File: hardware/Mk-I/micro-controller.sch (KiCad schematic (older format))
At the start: 29 parts, among them U10 STM32_SWD_Connector, U4 STM32F407VG, U8 MOLEX_microSD_47219-2001, X1 CRYSTAL

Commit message: Cleanup schematics
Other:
- note added: "Debug port"
- note added: "I2C pull-ups"
- note added: "SD card"
- moved on the sheet: U10, U8

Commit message: HW: Add a DFU mode switch
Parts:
- added DFU_MODE1: Jumper_NO_Small, Buttons_Switches_SMD:SW_SPST_EVQP7A, symbol Jumper_NO_Small
- C12, C13, C14, C15, C16, C17, C18, C19, C20, C21, C22, C23, C24, C4, C5: symbol C -> C-RESCUE-wnm_mk_1
- R10, R11, R12, R13, R14, R3, R4, R5, R6: symbol R -> R-RESCUE-wnm_mk_1
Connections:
- net labels added: BOOT0
- wire segments 44 -> 45

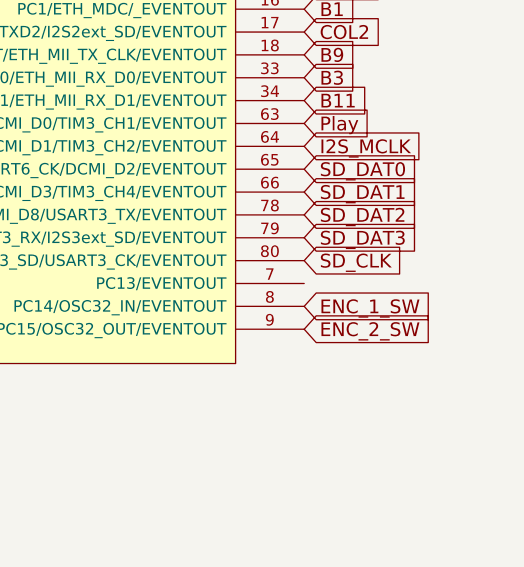
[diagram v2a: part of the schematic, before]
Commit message: HW: Add screen reset line and some ground path tweaking
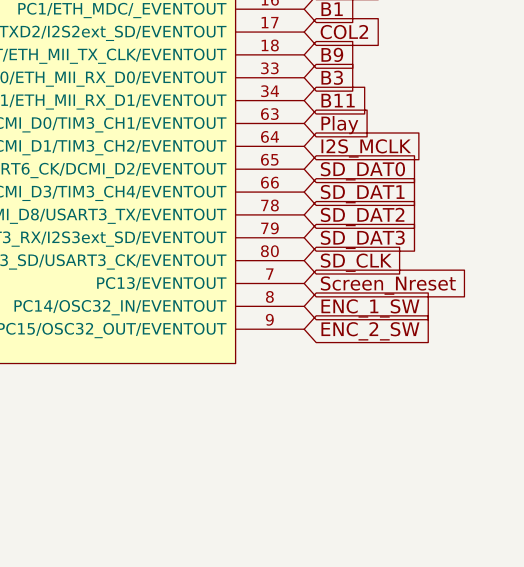
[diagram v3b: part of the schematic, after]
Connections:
- net Screen_Nreset: now reaches U4.7 (PC13/EVENTOUT)
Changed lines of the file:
@@
 Text GLabel 2300 1800 2    60   Input ~ 0
 3V3
+Text GLabel 12850 7200 2    60   Input ~ 0
+Screen_Nreset
 $EndSCHEMATC

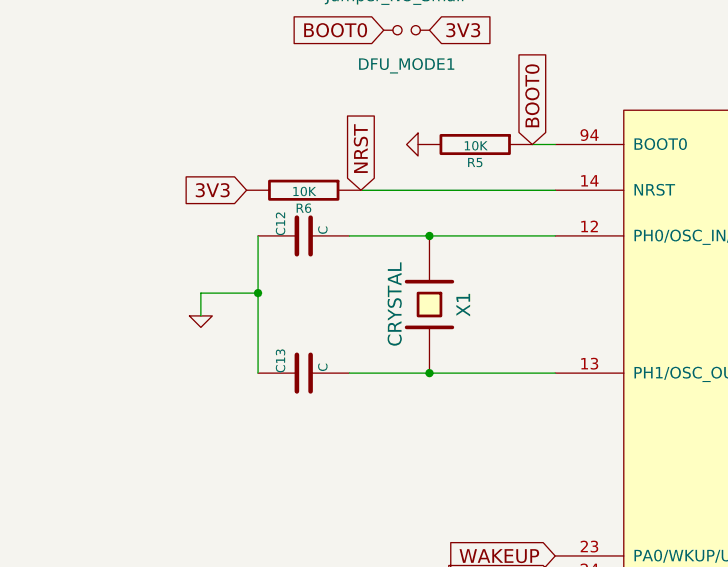
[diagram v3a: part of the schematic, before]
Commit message: HW: Start Mk-I rev-A known problems
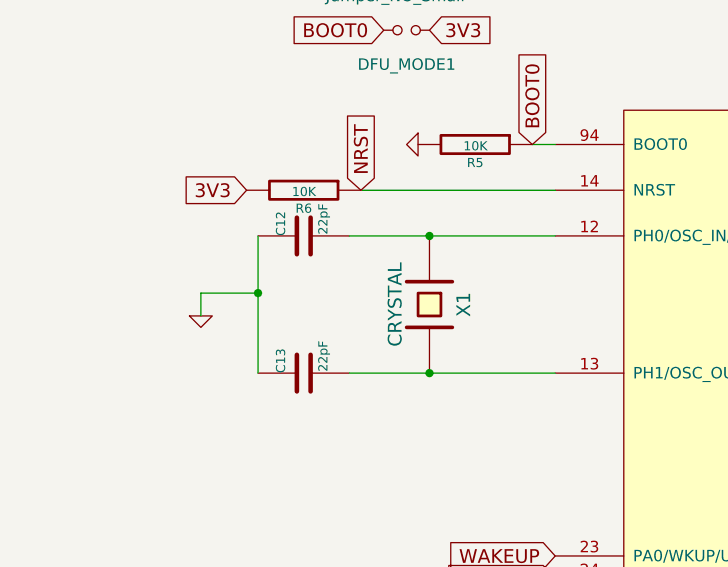
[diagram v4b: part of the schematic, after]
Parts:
- C12, C13: value C -> 22pF
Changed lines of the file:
@@
 AR Path="/585DBE08/585F8833" Ref="C12"  Part="1"
 F 0 "C12" H 1750 2800 40  0000 L CNN
-F 1 "C" H 1756 2615 40  0000 L CNN
+F 1 "22pF" H 1756 2615 40  0000 L CNN
 F 2 "Capacitors_SMD:C_0805" H 1788 2550 30  0001 C CNN
 F 3 "" H 1750 2700 60  0000 C CNN
@@
 AR Path="/585DBE08/585F888D" Ref="C13"  Part="1"
 F 0 "C13" H 1750 3400 40  0000 L CNN
-F 1 "C" H 1756 3215 40  0000 L CNN
+F 1 "22pF" H 1756 3215 40  0000 L CNN
 F 2 "Capacitors_SMD:C_0805" H 1788 3150 30  0001 C CNN
 F 3 "" H 1750 3300 60  0000 C CNN

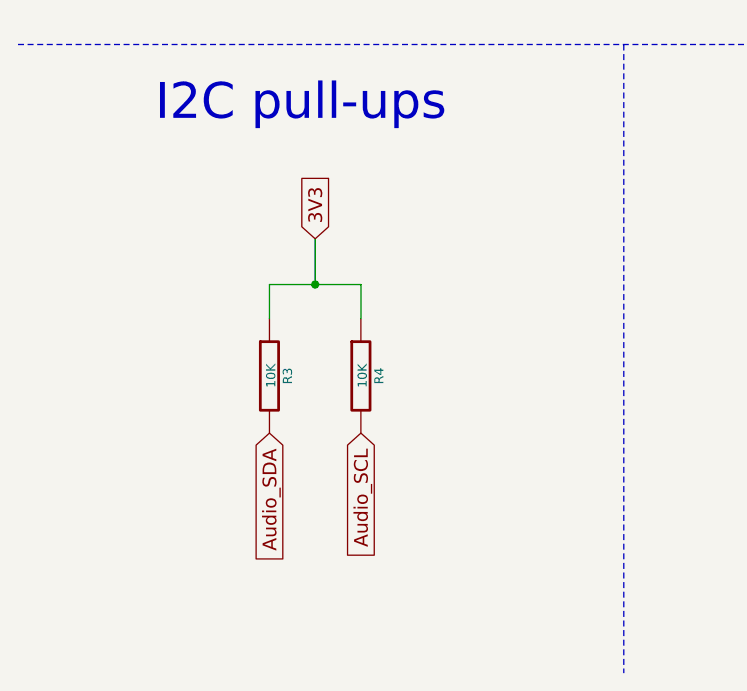
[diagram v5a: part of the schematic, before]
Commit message: HW: Add I2C debug/extension connector
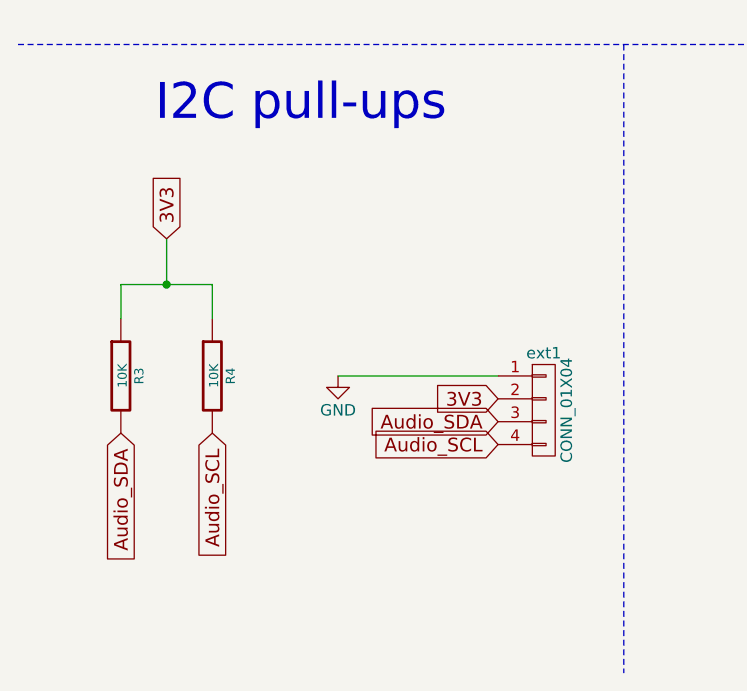
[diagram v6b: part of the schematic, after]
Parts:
- added ext1: CONN_01X04, Socket_Strips:Socket_Strip_Straight_1x04, symbol CONN_01X04
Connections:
- net 3V3: now also ext1.2 (P2)
- net Audio_SCL: now also ext1.4 (P4)
- net Audio_SDA: now also ext1.3 (P3)
- net GND: now also ext1.1 (P1)
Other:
- moved on the sheet: R3, R4
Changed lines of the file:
@@
 	1    0    0    -1
 $EndComp
-Text GLabel 1800 9300 1    60   Input ~ 0
+Text GLabel 1150 9300 1    60   Input ~ 0
 3V3
 $Comp
 L R-RESCUE-wnm_mk_1 R3
 U 1 1 586150DA
-P 1600 9900
+P 950 9900
 AR Path="/586150DA" Ref="R3"  Part="1"
 AR Path="/585DBE08/586150DA" Ref="R3"  Part="1"
-F 0 "R3" V 1680 9900 40  0000 C CNN
-F 1 "10K" V 1607 9901 40  0000 C CNN
-F 2 "Resistors_SMD:R_0805" V 1530 9900 30  0001 C CNN
-F 3 "" H 1600 9900 30  0000 C CNN
-	1    1600 9900
+F 0 "R3" V 1030 9900 40  0000 C CNN
+F 1 "10K" V 957 9901 40  0000 C CNN
+F 2 "Resistors_SMD:R_0805" V 880 9900 30  0001 C CNN
+F 3 "" H 950 9900 30  0000 C CNN
+	1    950  9900
 	1    0    0    -1
 $EndComp
@@
 L R-RESCUE-wnm_mk_1 R4
 U 1 1 58615169
-P 2000 9900
+P 1350 9900
 AR Path="/58615169" Ref="R4"  Part="1"
 AR Path="/585DBE08/58615169" Ref="R4"  Part="1"
-F 0 "R4" V 2080 9900 40  0000 C CNN
-F 1 "10K" V 2007 9901 40  0000 C CNN
-F 2 "Resistors_SMD:R_0805" V 1930 9900 30  0001 C CNN
-F 3 "" H 2000 9900 30  0000 C CNN
-	1    2000 9900
-	1    0    0    -1
-$EndComp
-Text GLabel 1600 10150 3    60   Input ~ 0
+F 0 "R4" V 1430 9900 40  0000 C CNN
+F 1 "10K" V 1357 9901 40  0000 C CNN
+F 2 "Resistors_SMD:R_0805" V 1280 9900 30  0001 C CNN
+F 3 "" H 1350 9900 30  0000 C CNN
+	1    1350 9900
+	1    0    0    -1
+$EndComp
+Text GLabel 950  10150 3    60   Input ~ 0
 Audio_SDA
-Text GLabel 2000 10150 3    60   Input ~ 0
+Text GLabel 1350 10150 3    60   Input ~ 0
 Audio_SCL
 Text GLabel 2850 5600 0    60   Input ~ 0
@@
 	1900 6100 1900 6300
 Wire Wire Line
-	1800 9300 1800 9500
-Connection ~ 1800 9500
-Wire Wire Line
-	2000 9500 2000 9650
-Wire Wire Line
-	2000 9500 1600 9500
-Wire Wire Line
-	1600 9500 1600 9650
+	1150 9300 1150 9500
+Connection ~ 1150 9500
+Wire Wire Line
+	1350 9500 1350 9650
+Wire Wire Line
+	1350 9500 950  9500
+Wire Wire Line
+	950  9500 950  9650
 Wire Wire Line
 	7250 9900 6300 9900
@@
 Text GLabel 12850 7200 2    60   Input ~ 0
 Screen_Nreset
+$Comp
+L CONN_01X04 ext1
+U 1 1 58C40226
+P 2800 10050
+F 0 "ext1" H 2800 10300 50  0000 C CNN
+F 1 "CONN_01X04" V 2900 10050 50  0000 C CNN
+F 2 "Socket_Strips:Socket_Strip_Straight_1x04" H 2800 10050 50  0001 C CNN
+F 3 "" H 2800 10050 50  0000 C CNN
+	1    2800 10050
+	1    0    0    -1
+$EndComp
+Text GLabel 2600 10200 0    60   Input ~ 0
+Audio_SCL
+Text GLabel 2600 10100 0    60   Input ~ 0
+Audio_SDA
+Text GLabel 2600 10000 0    60   Input ~ 0
+3V3
+$Comp
+L GND #PWR031
+U 1 1 58C40EDF
+P 1900 9900
+F 0 "#PWR031" H 1900 9650 50  0001 C CNN
+F 1 "GND" H 1900 9750 50  0000 C CNN
+F 2 "" H 1900 9900 50  0000 C CNN
+F 3 "" H 1900 9900 50  0000 C CNN
+	1    1900 9900
+	1    0    0    -1
+$EndComp
+Wire Wire Line
+	2600 9900 1900 9900
 $EndSCHEMATC

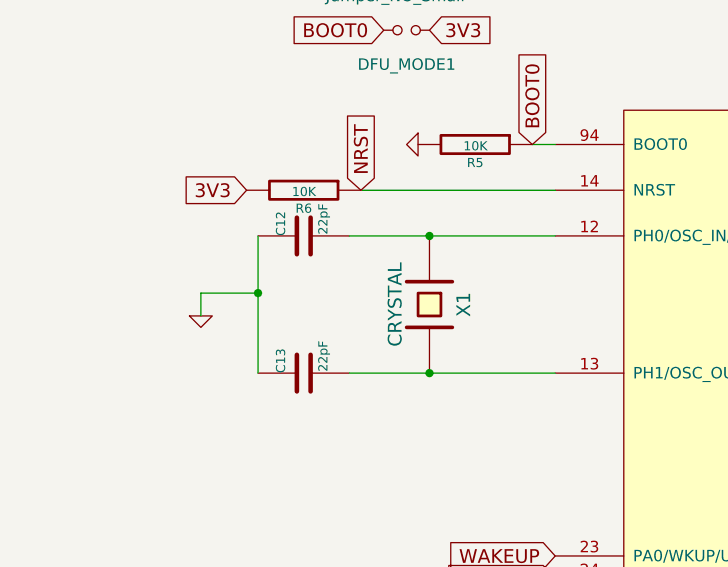
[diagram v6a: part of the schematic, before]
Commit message: HW: Improve oscillator layout
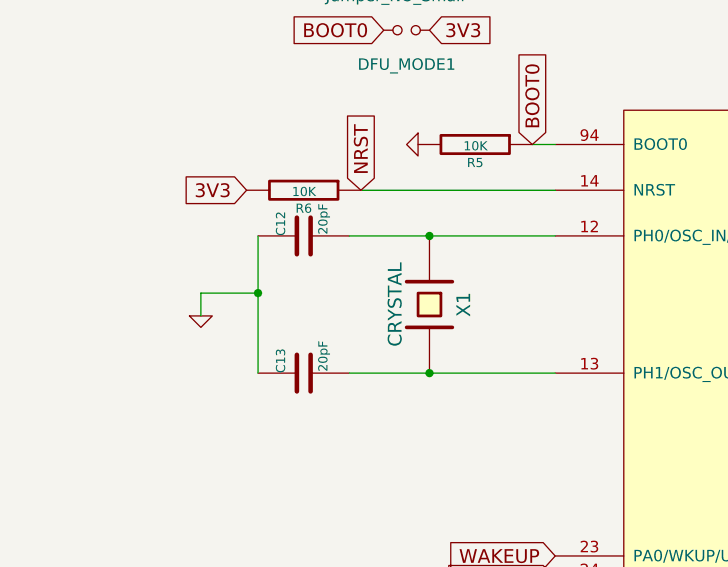
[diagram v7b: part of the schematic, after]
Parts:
- C12, C13: value 22pF -> 20pF
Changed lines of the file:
@@
 AR Path="/585DBE08/585F8833" Ref="C12"  Part="1"
 F 0 "C12" H 1750 2800 40  0000 L CNN
-F 1 "22pF" H 1756 2615 40  0000 L CNN
+F 1 "20pF" H 1756 2615 40  0000 L CNN
 F 2 "Capacitors_SMD:C_0805" H 1788 2550 30  0001 C CNN
 F 3 "" H 1750 2700 60  0000 C CNN
@@
 AR Path="/585DBE08/585F888D" Ref="C13"  Part="1"
 F 0 "C13" H 1750 3400 40  0000 L CNN
-F 1 "22pF" H 1756 3215 40  0000 L CNN
+F 1 "20pF" H 1756 3215 40  0000 L CNN
 F 2 "Capacitors_SMD:C_0805" H 1788 3150 30  0001 C CNN
 F 3 "" H 1750 3300 60  0000 C CNN
@@
 	1    0    0    -1
 $EndComp
-Wire Wire Line
-	1950 2700 2850 2700
-Wire Wire Line
-	1950 3300 2850 3300
-Connection ~ 2300 2700
-Connection ~ 2300 3300
-Wire Wire Line
-	1550 3300 1550 2700
-Wire Wire Line
-	1550 2950 1300 2950
-Wire Wire Line
-	1300 2950 1300 3050
-Connection ~ 1550 2950
-Wire Wire Line
-	8600 1700 8600 1850
-Wire Wire Line
-	8300 1700 8300 1850
-Wire Wire Line
-	8000 1700 8000 1850
-Wire Wire Line
-	7700 1700 7700 1850
-Wire Wire Line
-	7400 1700 7400 1850
-Wire Wire Line
-	7100 1700 7100 1850
-Wire Wire Line
-	9100 1750 9100 1850
-Connection ~ 8600 1750
-Connection ~ 8300 1750
-Connection ~ 8000 1750
-Connection ~ 7700 1750
-Connection ~ 7400 1750
-Connection ~ 7100 1750
-Wire Wire Line
-	6800 1750 6800 1700
-Wire Wire Line
-	8600 1150 8600 1300
-Wire Wire Line
-	6800 1150 6800 1300
-Connection ~ 6800 1750
-Wire Wire Line
-	6100 1700 6100 1850
-Wire Wire Line
-	6100 1150 6100 1300
-Connection ~ 6800 1150
-Wire Wire Line
-	7100 1300 7100 1150
-Connection ~ 7100 1150
-Wire Wire Line
-	7400 1300 7400 1150
-Connection ~ 7400 1150
-Wire Wire Line
-	7700 1300 7700 1150
-Connection ~ 7700 1150
-Wire Wire Line
-	8000 1300 8000 1150
-Connection ~ 8000 1150
-Wire Wire Line
-	8300 1300 8300 1150
-Connection ~ 8300 1150
-Wire Wire Line
-	5450 1150 8600 1150
-Wire Wire Line
-	5600 1150 5600 1300
-Connection ~ 6100 1150
-Wire Wire Line
-	5600 1700 5600 1850
-Wire Wire Line
-	5300 1750 6100 1750
-Connection ~ 5600 1750
-Connection ~ 6100 1750
-Wire Wire Line
-	4800 1750 4550 1750
-Connection ~ 5600 1150
-Wire Wire Line
-	2850 6100 1900 6100
-Wire Wire Line
-	1900 6100 1900 6300
-Wire Wire Line
-	1150 9300 1150 9500
-Connection ~ 1150 9500
-Wire Wire Line
-	1350 9500 1350 9650
-Wire Wire Line
-	1350 9500 950  9500
-Wire Wire Line
-	950  9500 950  9650
-Wire Wire Line
-	7250 9900 6300 9900
-Wire Wire Line
-	6300 9900 6300 10150
-Wire Wire Line
-	5450 9200 5450 10325
-Connection ~ 5450 9950
-Connection ~ 5450 10100
-Connection ~ 5450 9800
-Connection ~ 5450 9500
-Connection ~ 5450 10250
 $Comp
 L C-RESCUE-wnm_mk_1 C24
@@
 	1    0    0    -1
 $EndComp
-Wire Wire Line
-	6900 9725 6900 9900
-Connection ~ 6900 9900
-Wire Wire Line
-	7800 9650 7800 9325
-Wire Wire Line
-	7800 9325 6900 9325
-Wire Wire Line
-	7350 9200 7350 9325
-Connection ~ 7350 9325
 Text GLabel 2850 4600 0    60   Input ~ 0
 ENC_1_A
@@
 	1    0    0    -1
 $EndComp
-Wire Wire Line
-	9900 9850 9900 9800
-Wire Wire Line
-	9900 9800 10000 9800
 Text GLabel 10000 9600 0    60   Input ~ 0
 SWCLK
 Text GLabel 10000 10000 0    60   Input ~ 0
 SWDIO
-Wire Wire Line
-	2000 2500 2850 2500
 Text GLabel 2000 2500 1    60   Input ~ 0
 NRST
 Text GLabel 10000 10200 0    60   Input ~ 0
 NRST
-Wire Wire Line
-	6800 1750 8600 1750
 Text GLabel 9100 1750 1    60   Input ~ 0
 VBAT
-Wire Notes Line
-	500  8450 11700 8450
-Wire Notes Line
-	3150 8450 3150 11200
-Wire Notes Line
-	9000 8450 9000 11200
-Wire Notes Line
-	11700 8450 11700 11200
 Text Notes 1100 8800 0    157  ~ 0
 I2C pull-ups
@@
 Text Notes 9750 8750 0    157  ~ 0
 Debug port
-Wire Wire Line
-	2850 2300 2750 2300
 Text GLabel 2750 2300 1    60   Input ~ 0
 BOOT0
@@
 $EndComp
 Wire Wire Line
+	1950 2700 2850 2700
+Wire Wire Line
+	1950 3300 2850 3300
+Connection ~ 2300 2700
+Connection ~ 2300 3300
+Wire Wire Line
+	1550 3300 1550 2700
+Wire Wire Line
+	1550 2950 1300 2950
+Wire Wire Line
+	1300 2950 1300 3050
+Connection ~ 1550 2950
+Wire Wire Line
+	8600 1700 8600 1850
+Wire Wire Line
+	8300 1700 8300 1850
+Wire Wire Line
+	8000 1700 8000 1850
+Wire Wire Line
+	7700 1700 7700 1850
+Wire Wire Line
+	7400 1700 7400 1850
+Wire Wire Line
+	7100 1700 7100 1850
+Wire Wire Line
+	9100 1750 9100 1850
+Connection ~ 8600 1750
+Connection ~ 8300 1750
+Connection ~ 8000 1750
+Connection ~ 7700 1750
+Connection ~ 7400 1750
+Connection ~ 7100 1750
+Wire Wire Line
+	6800 1750 6800 1700
+Wire Wire Line
+	8600 1150 8600 1300
+Wire Wire Line
+	6800 1150 6800 1300
+Connection ~ 6800 1750
+Wire Wire Line
+	6100 1700 6100 1850
+Wire Wire Line
+	6100 1150 6100 1300
+Connection ~ 6800 1150
+Wire Wire Line
+	7100 1300 7100 1150
+Connection ~ 7100 1150
+Wire Wire Line
+	7400 1300 7400 1150
+Connection ~ 7400 1150
+Wire Wire Line
+	7700 1300 7700 1150
+Connection ~ 7700 1150
+Wire Wire Line
+	8000 1300 8000 1150
+Connection ~ 8000 1150
+Wire Wire Line
+	8300 1300 8300 1150
+Connection ~ 8300 1150
+Wire Wire Line
+	5450 1150 8600 1150
+Wire Wire Line
+	5600 1150 5600 1300
+Connection ~ 6100 1150
+Wire Wire Line
+	5600 1700 5600 1850
+Wire Wire Line
+	5300 1750 6100 1750
+Connection ~ 5600 1750
+Connection ~ 6100 1750
+Wire Wire Line
+	4800 1750 4550 1750
+Connection ~ 5600 1150
+Wire Wire Line
+	2850 6100 1900 6100
+Wire Wire Line
+	1900 6100 1900 6300
+Wire Wire Line
+	1150 9300 1150 9500
+Connection ~ 1150 9500
+Wire Wire Line
+	1350 9500 1350 9650
+Wire Wire Line
+	1350 9500 950  9500
+Wire Wire Line
+	950  9500 950  9650
+Wire Wire Line
+	7250 9900 6300 9900
+Wire Wire Line
+	6300 9900 6300 10150
+Wire Wire Line
+	5450 9200 5450 10325
+Connection ~ 5450 9950
+Connection ~ 5450 10100
+Connection ~ 5450 9800
+Connection ~ 5450 9500
+Connection ~ 5450 10250
+Wire Wire Line
+	6900 9725 6900 9900
+Connection ~ 6900 9900
+Wire Wire Line
+	7800 9650 7800 9325
+Wire Wire Line
+	7800 9325 6900 9325
+Wire Wire Line
+	7350 9200 7350 9325
+Connection ~ 7350 9325
+Wire Wire Line
+	9900 9850 9900 9800
+Wire Wire Line
+	9900 9800 10000 9800
+Wire Wire Line
+	2000 2500 2850 2500
+Wire Wire Line
+	6800 1750 8600 1750
+Wire Notes Line
+	500  8450 11700 8450
+Wire Notes Line
+	3150 8450 3150 11200
+Wire Notes Line
+	9000 8450 9000 11200
+Wire Notes Line
+	11700 8450 11700 11200
+Wire Wire Line
+	2850 2300 2750 2300
+Wire Wire Line
 	2600 9900 1900 9900

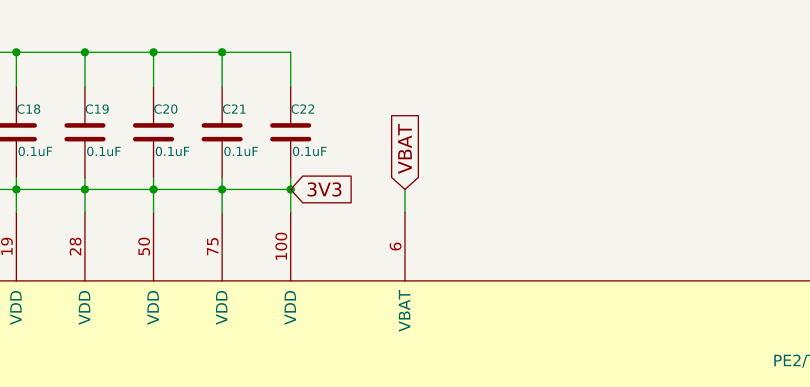
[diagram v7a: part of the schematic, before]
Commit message: HW: Divide VBAT before connecting to the MCU
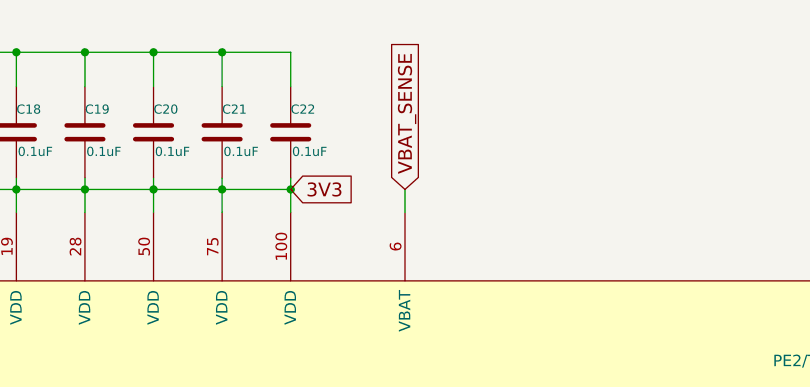
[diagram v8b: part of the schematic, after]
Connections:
- net VBAT renamed VBAT_SENSE
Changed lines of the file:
@@
 NRST
 Text GLabel 9100 1750 1    60   Input ~ 0
-VBAT
+VBAT_SENSE
 Text Notes 1100 8800 0    157  ~ 0
 I2C pull-ups
